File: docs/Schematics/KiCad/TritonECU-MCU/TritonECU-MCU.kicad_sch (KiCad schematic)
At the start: 38 parts, among them J1 Header A, J2 Header B, J3 Header C, J4 Header D, J5 SWD TC2030, U1 STM32F767ZIT6, Y1 8MHz, Y2 32.768kHz

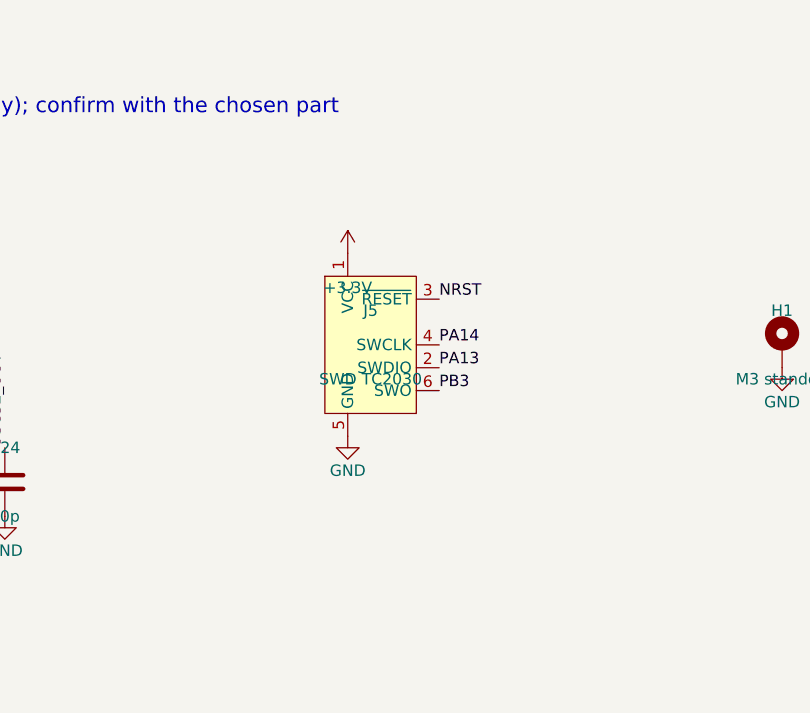
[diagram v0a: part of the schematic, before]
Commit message: MCU module: place 6-layer PCB with Samtec SMT headers and STDC14
gen_module_pcb.py builds the 44 x 44 mm, 6-layer module board in KiCad's
Python. The stack is F sig / In1 GND / In2 sig / In3 sig / In4 +3.3V / B sig.
The F767 is on top; decoupling, crystals and the headers are on the bottom.

The headers are Samtec TFM-118-22-L-D-A (module bottom) and
SFM-118-02-S-D-A-N-K-TR (carrier top), both SMT. Pad geometry and alignment
holes come from the vendor footprints imported via Component Search Engine;
positions come from mcu_pinout.py, and the rows now sit at 16.5 mm so the TFM
bodies clear at the corners. The carrier DB3 footprint is regenerated to match,
and all 144 pins are verified to mate.

The H1 standoff is offset 0.7 mm per axis, so the module fits only one way
round: the no-notch socket and four identical headers give no polarization.

An STDC14 programming header (FTSH-107, SMT) on the module top carries SWD,
SWO, NRST and the ST-Link VCP on USART3 PD8/PD9. Passives use hand-solder
footprints.

Co-Authored-By: Claude Opus 5.5 <noreply@anthropic.com>
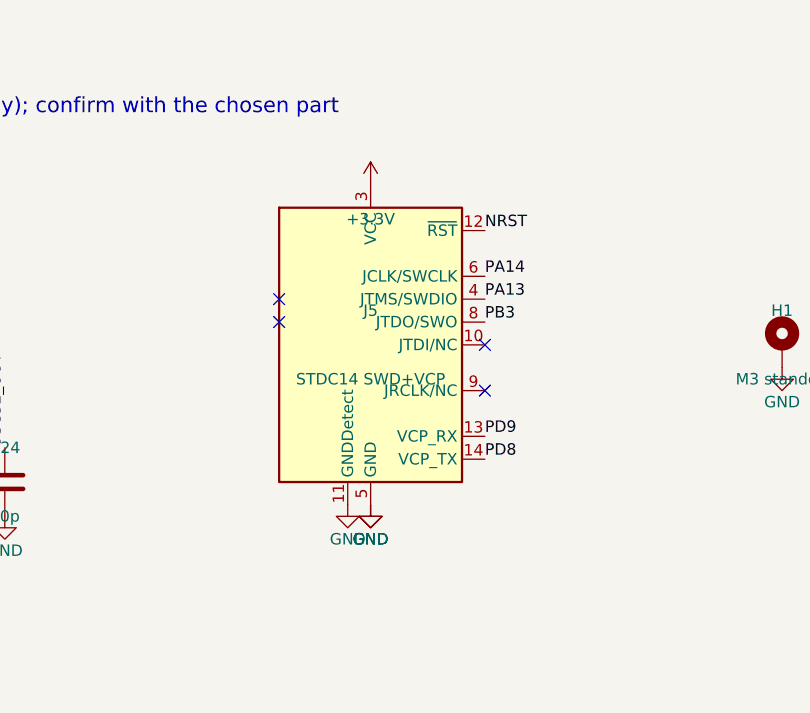
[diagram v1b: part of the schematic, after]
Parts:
- removed J5: SWD TC2030, Connector:Tag-Connect_TC2030-IDC-NL_2x03_P1.27mm_Vertical, symbol Connector:Conn_ARM_SWD_TagConnect_TC2030
- added J5: STDC14 SWD+VCP, Connector_PinHeader_1.27mm:PinHeader_2x07_P1.27mm_Vertical_SMD, symbol Connector:Conn_ST_STDC14
- C1, C10, C11, C12, C15, C16, C19, C2, C20, C21, C22, C23, C24, C3, C4, C5, C6, C7, C8, C9: footprint Capacitor_SMD:C_0402_1005Metric -> Capacitor_SMD:C_0402_1005Metric_Pad0.74x0.62mm_HandSolder
- C13, C17, C18: footprint Capacitor_SMD:C_0603_1608Metric -> Capacitor_SMD:C_0603_1608Metric_Pad1.08x0.95mm_HandSolder
- C14: footprint Capacitor_SMD:C_0805_2012Metric -> Capacitor_SMD:C_0805_2012Metric_Pad1.18x1.45mm_HandSolder
- FB1: footprint Inductor_SMD:L_0603_1608Metric -> Inductor_SMD:L_0603_1608Metric_Pad1.05x0.95mm_HandSolder
- H1, H2, H3, H4: now left out of the parts list
- J1, J2, J3, J4: footprint Connector_PinHeader_1.27mm:PinHeader_2x18_P1.27mm_Vertical -> TritonECU-MCU:Samtec_TFM-118-22-L-D-A; Mate SFM-118-02-L-D-A on the carrier, 9.91 mm mated (Samtec TFM-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 -> SFM-118-02-S-D-A-N-K-TR on the carrier, 9.91 mm mated (Samt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
- R1: footprint Resistor_SMD:R_0402_1005Metric -> Resistor_SMD:R_0402_1005Metric_Pad0.72x0.64mm_HandSolder
- Y1: footprint Crystal:Crystal_SMD_3225-4Pin_3.2x2.5mm -> Crystal:Crystal_SMD_3225-4Pin_3.2x2.5mm_HandSoldering
- Y2: footprint Crystal:Crystal_SMD_2012-2Pin_2.0x1.2mm -> Crystal:Crystal_SMD_2012-2Pin_2.0x1.2mm_HandSoldering
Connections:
- net +3.3V: now also J5.3 (VCC)
- net GND: now also J5.11 (GNDDetect), J5.5 (GND), J5.7 (GND)
- net NRST: now also J5.12 (~{RST})
- net PA13: now also J5.4 (JTMS/SWDIO)
- net PA14: now also J5.6 (JCLK/SWCLK)
- net PB3: now also J5.8 (JTDO/SWO)
- net PD8: now also J5.14 (VCP_TX)
- net PD9: now also J5.13 (VCP_RX)
- no-connect marks 0 -> 4

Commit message: MCU module: route 46 mm board on Samtec FTSH/FLE with Wurth/PEM standoffs
- Interconnect: FTSH-118-02-L-DV-A (module bottom) mating FLE-118-01-G-DV-K-TR
  (carrier top), 7.47 mm stack, replacing TFM-118-22 / SFM-118-02. FTSH pads
  trimmed 0.1 mm at the inner end for the 0.25 mm hole clearance to the -A
  alignment holes.
- Standoffs: Wurth 9774050982R 5 mm SMT spacer on the module, PEM
  SMTSO-M3-2ET 2 mm on the carrier, 0.5 mm M3 washer between (7.5 mm),
  M3 x 10 screw. Spacer footprint generated from the Wurth land pattern with
  a GND ring, plus Wurth's STEP model.
- Module grows 44 -> 46 mm for the spacer pads; H1 keying offset now inward.
- Board routed with Freerouting: DRC 0 violations, 0 unconnected, schematic
  parity clean. All parts included in the BOM; supplier BOM exports added.
- Generators: fix footprint-to-symbol links (netlist tstamps regex), copy all
  schematic fields, skip no-connect pins, footprint-only mode in gen_module.py,
  carrier floor plan refreshes a changed mate footprint in place.

Co-Authored-By: Claude Opus 5.5 <noreply@anthropic.com>
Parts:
- C1, C10, C11, C12, C16, C19, C2, C20, C3, C4, C5, C6, C7, C8, C9: Manufacturer_Name (none) -> Murata Electronics; Manufacturer_Part_Number (none) -> GCM155L8EH104KE07D; Mouser Part Number (none) -> 81-GCM155L8EH104KE7D; Mouser Price/Stock (none) -> https://www.mouser.com/en/ProductDetail/Murata-Electronics/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
- C13: Manufacturer_Name (none) -> Murata Electronics; Manufacturer_Part_Number (none) -> GRM188C71A475ME11D; Mouser Part Number (none) -> 81-GRM188C71A475ME1D; Mouser Price/Stock (none) -> https://www.mouser.com/en/ProductDetail/Murata-Electronics/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
- C14: Manufacturer_Name (none) -> TAIYO YUDEN; Manufacturer_Part_Number (none) -> MCASL21GBB7106KTNA01; Mouser Part Number (none) -> 963-MCASL21GBB7106KT; Mouser Price/Stock (none) -> https://www.mouser.com/en/ProductDetail/TAIYO-YUDEN/MCASL21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
- C15: Manufacturer_Name (none) -> KYOCERA AVX; Manufacturer_Part_Number (none) -> KAM05CR71A105KH; Mouser Part Number (none) -> 581-KAM05CR71A105KH; Mouser Price/Stock (none) -> https://www.mouser.com/en/ProductDetail/KYOCERA-AVX/KAM05CR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
- C17, C18: Manufacturer_Name (none) -> KYOCERA AVX; Manufacturer_Part_Number (none) -> KGM15BR71A225KT; Mouser Part Number (none) -> 581-KGM15BR71A225KT; Mouser Price/Stock (none) -> https://www.mouser.com/en/ProductDetail/KYOCERA-AVX/KGM15BR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
- C21, C22: value 10p -> 27p; Manufacturer_Name (none) -> KEMET; Manufacturer_Part_Number (none) -> C0402C270F4HACAUTO; Mouser Part Number (none) -> 80-C0402C270F4HAUTO; Mouser Price/Stock (none) -> https://www.mouser.com/en/ProductDetail/KEMET/C0402C270F4HA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
- C23, C24: value 10p -> 18p; Manufacturer_Name (none) -> YAGEO; Manufacturer_Part_Number (none) -> AC0402GRNPO9BN180; Mouser Part Number (none) -> 603-AC0402GRNPO9BN18; Mouser Price/Stock (none) -> https://www.mouser.com/en/ProductDetail/YAGEO/AC0402GRNPO9B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
- FB1: Manufacturer_Name (none) -> Pulse Electronics; Manufacturer_Part_Number (none) -> BBPY00201209221Y00; Mouser Part Number (none) -> 603-BBPY201209221Y00; Mouser Price/Stock (none) -> https://www.mouser.com/en/ProductDetail/Pulse-Electronics/B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
- H1, H2, H3, H4: value M3 standoff -> Spacer 5mm; footprint MountingHole:MountingHole_3.2mm_M3_Pad_Via -> TritonECU-MCU:Wurth_WA-SMST_9774050982R; MPN (none) -> 9774050982R; Manufacturer (none) -> Wurth Elektronik; Manufacturer_Name (none) -> Wurth Elektronik; Manufacturer_Part_Number (none) -> 9774050982R; Note (none) -> WA-SMST SMT steel spacer 5 mm, module bottom; 2.5 mm M3 sta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; now in the parts list
- J1: value Header A -> (none); footprint TritonECU-MCU:Samtec_TFM-118-22-L-D-A -> TritonECU-MCU:Samtec_FTSH-118-02-L-DV-A; MPN TFM-118-22-L-D-A -> FTSH-118-02-L-DV-A; Manufacturer_Name (none) -> Samtec Inc.; Manufacturer_Part_Number (none) -> FTSH-118-02-L-DV-A; Mate SFM-118-02-S-D-A-N-K-TR on the carrier, 9.91 mm mated (Samt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 -> FLE-118-01-G-DV-K-TR on the carrier, 7.47 mm mated (Samtec 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; Note (none) -> Header A
- J2: value Header B -> (none); footprint TritonECU-MCU:Samtec_TFM-118-22-L-D-A -> TritonECU-MCU:Samtec_FTSH-118-02-L-DV-A; MPN TFM-118-22-L-D-A -> FTSH-118-02-L-DV-A; Manufacturer_Name (none) -> Samtec Inc.; Manufacturer_Part_Number (none) -> FTSH-118-02-L-DV-A; Mate SFM-118-02-S-D-A-N-K-TR on the carrier, 9.91 mm mated (Samt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 -> FLE-118-01-G-DV-K-TR on the carrier, 7.47 mm mated (Samtec 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; Note (none) -> Header B
- J3: value Header C -> (none); footprint TritonECU-MCU:Samtec_TFM-118-22-L-D-A -> TritonECU-MCU:Samtec_FTSH-118-02-L-DV-A; MPN TFM-118-22-L-D-A -> FTSH-118-02-L-DV-A; Manufacturer_Name (none) -> Samtec Inc.; Manufacturer_Part_Number (none) -> FTSH-118-02-L-DV-A; Mate SFM-118-02-S-D-A-N-K-TR on the carrier, 9.91 mm mated (Samt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 -> FLE-118-01-G-DV-K-TR on the carrier, 7.47 mm mated (Samtec 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; Note (none) -> Header C
- J4: value Header D -> (none); footprint TritonECU-MCU:Samtec_TFM-118-22-L-D-A -> TritonECU-MCU:Samtec_FTSH-118-02-L-DV-A; MPN TFM-118-22-L-D-A -> FTSH-118-02-L-DV-A; Manufacturer_Name (none) -> Samtec Inc.; Manufacturer_Part_Number (none) -> FTSH-118-02-L-DV-A; Mate SFM-118-02-S-D-A-N-K-TR on the carrier, 9.91 mm mated (Samt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 -> FLE-118-01-G-DV-K-TR on the carrier, 7.47 mm mated (Samtec 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; Note (none) -> Header D
- J5: Manufacturer_Name (none) -> Samtec; Manufacturer_Part_Number (none) -> FTSH-107-01-L-DV-K-A-TR; Mouser Part Number (none) -> 200-FTSH10701LDVKATR; Mouser Price/Stock (none) -> https://www.mouser.com/en/ProductDetail/Samtec/FTSH-107-01-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
- R1: Manufacturer_Name (none) -> YAGEO; Manufacturer_Part_Number (none) -> AT0402FRE0710KL; Mouser Part Number (none) -> 603-AT0402FRE0710KL; Mouser Price/Stock (none) -> https://www.mouser.com/en/ProductDetail/YAGEO/AT0402FRE0710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
- U1: Future Part Number (none) -> 3199333; Future Part URL (none) -> https://www.futureelectronics.com/p/semiconductors--microco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
- Y1: Manufacturer_Name (none) -> ABRACON; Manufacturer_Part_Number (none) -> ABM8AIG-8.000MHZ-1Z-T; Mouser Part Number (none) -> 815-M8AIG-8-1ZT; Mouser Price/Stock (none) -> https://www.mouser.com/en/ProductDetail/ABRACON/ABM8AIG-8.0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
- Y2: Manufacturer_Name (none) -> ECS; Manufacturer_Part_Number (none) -> ECS-.327-12.5-12QS-TR; Mouser Part Number (none) -> 520-.327-12.5-12QST; Mouser Price/Stock (none) -> https://www.mouser.com/en/ProductDetail/ECS/ECS-.327-12.5-1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
